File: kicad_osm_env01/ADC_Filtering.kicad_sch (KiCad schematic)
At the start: 16 parts

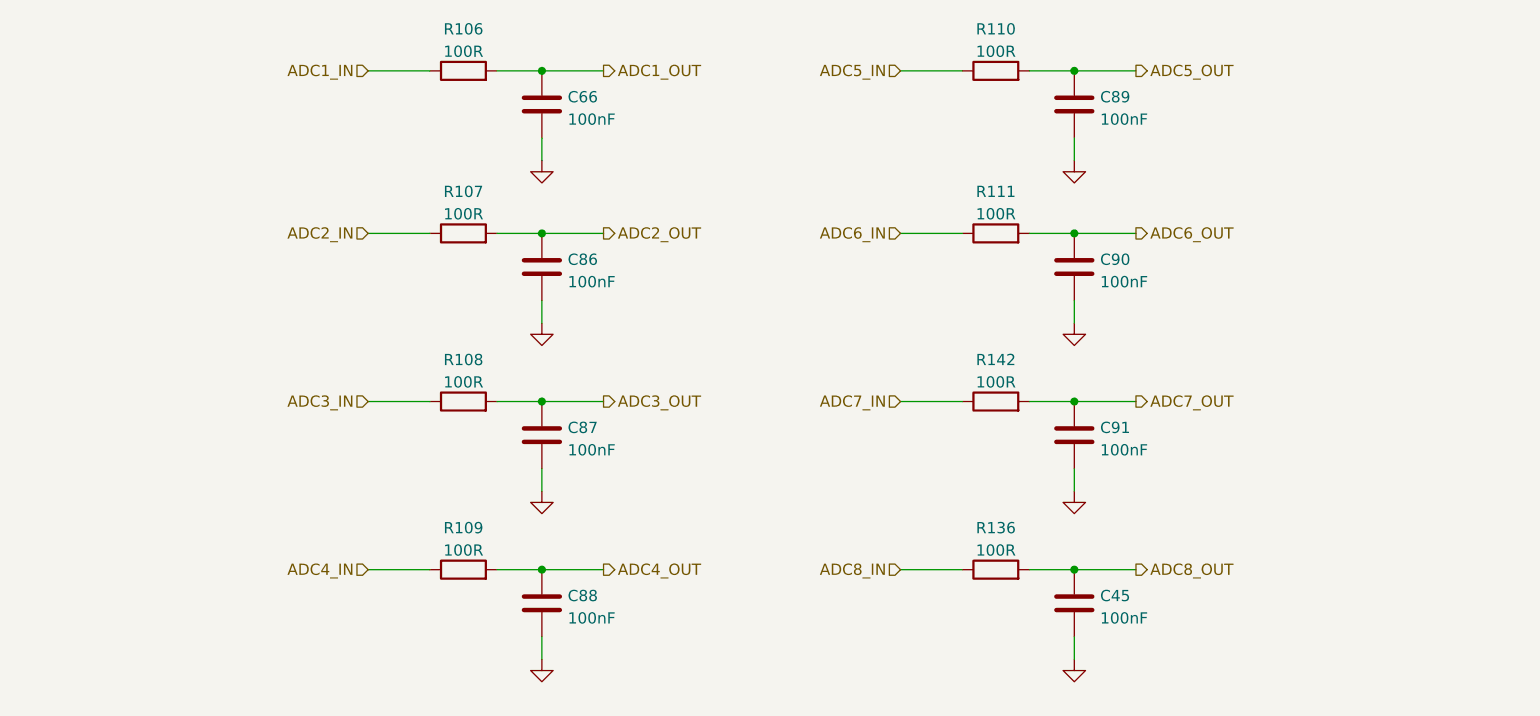
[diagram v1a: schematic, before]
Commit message: removed io module and 5V regulator
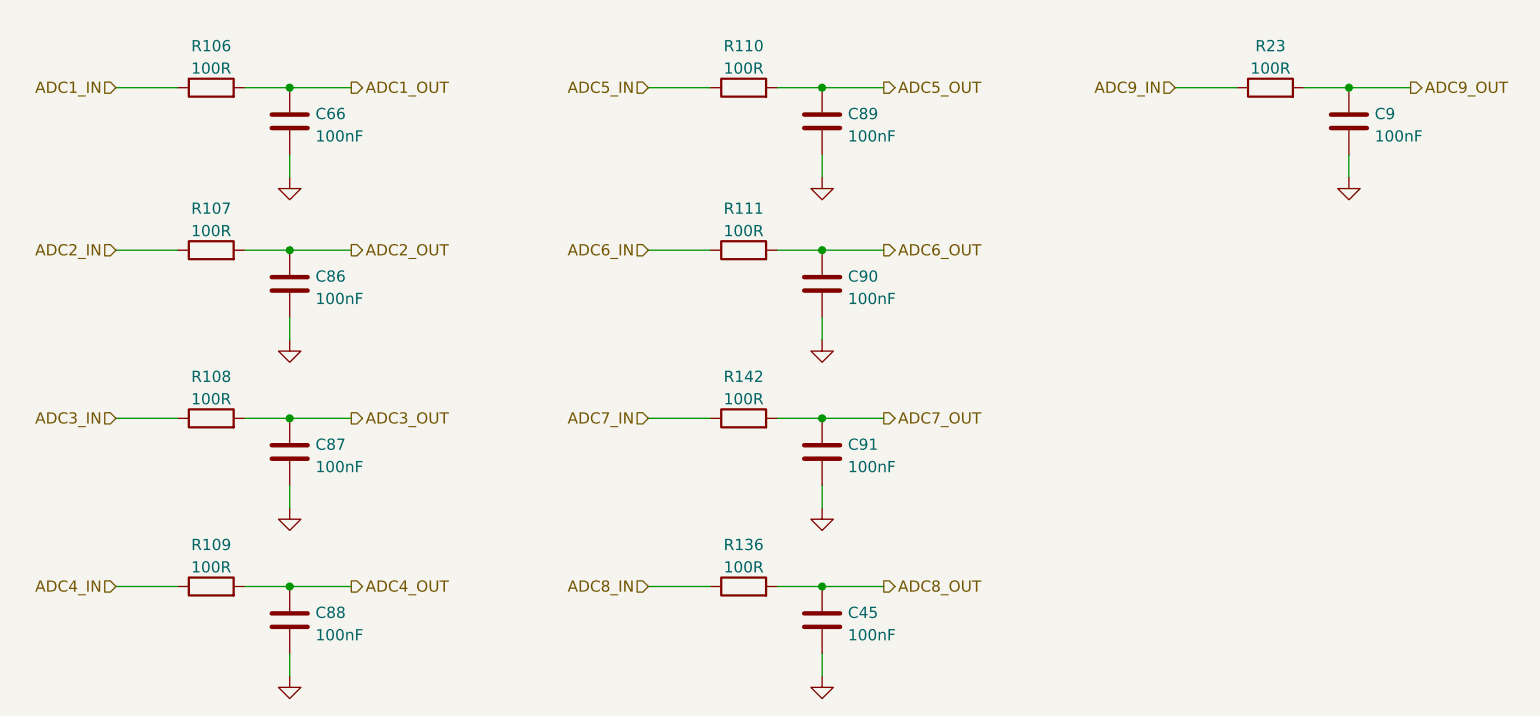
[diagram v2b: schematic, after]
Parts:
- added C9: 100nF, Capacitor_SMD:C_0402_1005Metric, symbol Device:C
- added R23: 100R, Resistor_SMD:R_0603_1608Metric, symbol Device:R
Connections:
- net GND: now also C9.2
- new net ADC9_IN: R23.1
- new net ADC9_OUT: C9.1, R23.2
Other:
- moved on the sheet: C45, C66, C86, C87, C88, C89, C90, C91, R106, R107, R108, R109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

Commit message: updated schematics with 5V ored circuit and new 3v3 regulator
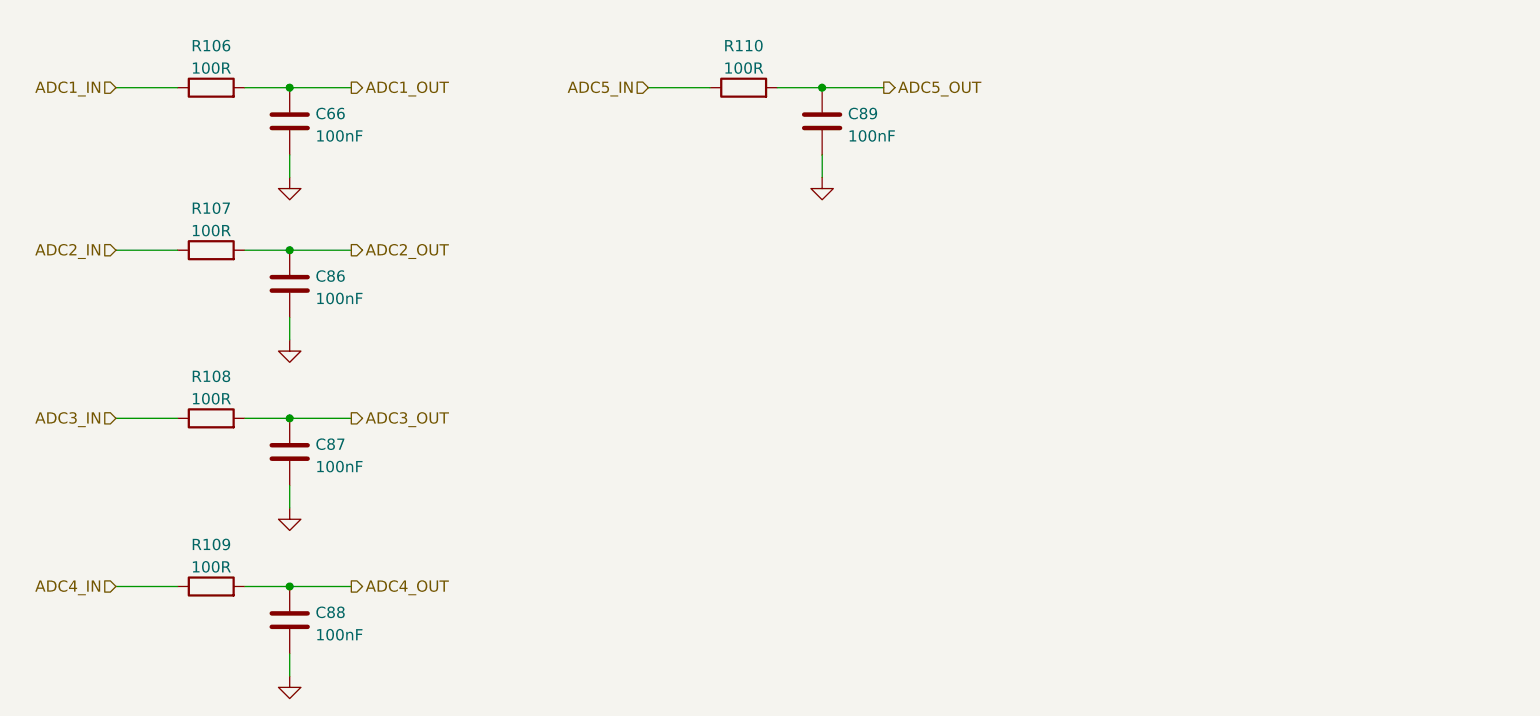
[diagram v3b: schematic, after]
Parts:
- removed C45, C9, C90, C91: 100nF, Capacitor_SMD:C_0402_1005Metric, symbol Device:C
- removed R111, R136, R142, R23: 100R, Resistor_SMD:R_0603_1608Metric, symbol Device:R

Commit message: assigned all footprints
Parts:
- C66, C86, C87, C88, C89: Voltage (none) -> 50V
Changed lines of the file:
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@@
   (title_block
     (title "Open Smart Monitor")
-    (date "2022-09-26")
-    (rev "C")
+    (date "2023-09-29")
+    (rev "C.2")
     (company "Devtank LTD")
     (comment 1 "Part No: 304-010")
@@
       (effects (font (size 1.27 1.27)) hide)
     )
-    (property "Datasheet" "~" (at 41.275 26.67 0)
+    (property "Datasheet" "" (at 41.275 26.67 0)
       (effects (font (size 1.27 1.27)) hide)
     )
@@
       (effects (font (size 1.27 1.27)) hide)
     )
-    (property "Datasheet" "~" (at 50.165 48.895 0)
+    (property "Datasheet" "" (at 50.165 48.895 0)
+      (effects (font (size 1.27 1.27)) hide)
+    )
+    (property "Voltage" "50V" (at 50.165 48.895 0)
       (effects (font (size 1.27 1.27)) hide)
     )
@@
       (effects (font (size 1.27 1.27)) hide)
     )
-    (property "Datasheet" "~" (at 101.6 26.67 0)
+    (property "Datasheet" "" (at 101.6 26.67 0)
       (effects (font (size 1.27 1.27)) hide)
     )
@@
       (effects (font (size 1.27 1.27)) hide)
     )
-    (property "Datasheet" "~" (at 41.275 64.135 0)
+    (property "Datasheet" "" (at 41.275 64.135 0)
       (effects (font (size 1.27 1.27)) hide)
     )
@@
       (effects (font (size 1.27 1.27)) hide)
     )
-    (property "Datasheet" "~" (at 41.275 83.185 0)
+    (property "Datasheet" "" (at 41.275 83.185 0)
       (effects (font (size 1.27 1.27)) hide)
     )
@@
       (effects (font (size 1.27 1.27)) hide)
     )
-    (property "Datasheet" "~" (at 50.165 30.48 0)
+    (property "Datasheet" "" (at 50.165 30.48 0)
+      (effects (font (size 1.27 1.27)) hide)
+    )
+    (property "Voltage" "50V" (at 50.165 30.48 0)
       (effects (font (size 1.27 1.27)) hide)
     )
@@
       (effects (font (size 1.27 1.27)) hide)
     )
-    (property "Datasheet" "~" (at 50.165 67.945 0)
+    (property "Datasheet" "" (at 50.165 67.945 0)
+      (effects (font (size 1.27 1.27)) hide)
+    )
+    (property "Voltage" "50V" (at 50.165 67.945 0)
       (effects (font (size 1.27 1.27)) hide)
     )
@@
       (effects (font (size 1.27 1.27)) hide)
     )
-    (property "Datasheet" "~" (at 50.165 86.995 0)
+    (property "Datasheet" "" (at 50.165 86.995 0)
+      (effects (font (size 1.27 1.27)) hide)
+    )
+    (property "Voltage" "50V" (at 50.165 86.995 0)
       (effects (font (size 1.27 1.27)) hide)
     )
@@
       (effects (font (size 1.27 1.27)) hide)
     )
-    (property "Datasheet" "~" (at 110.49 30.48 0)
+    (property "Datasheet" "" (at 110.49 30.48 0)
+      (effects (font (size 1.27 1.27)) hide)
+    )
+    (property "Voltage" "50V" (at 110.49 30.48 0)
       (effects (font (size 1.27 1.27)) hide)
     )
@@
       (effects (font (size 1.27 1.27)) hide)
     )
-    (property "Datasheet" "~" (at 41.275 45.085 0)
-      (effects (font (size 1.27 1.27)) hide)
-    )
+    (property "Datasheet" "" (at 41.275 45.085 0)
+      (effects (font (size 1.27 1.27)) hide)
+    )

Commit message: added information to symbol entries table, added jumper settings table, minor single track update on layout
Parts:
- C66, C86, C87, C88, C89: Characteristics (none) -> X5R; Other (none) -> Can use own part, but needs to meet the specs
- R106, R107, R108, R109, R110: Tolerance (none) -> 1%
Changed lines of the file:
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@@
+      (effects (font (size 1.27 1.27)) hide)
+    )
+    (property "Tolerance" "1%" (at 41.275 26.67 0)
+      (effects (font (size 1.27 1.27)) hide)
+    )
+    (property "Power Rating" "" (at 41.275 26.67 0)
+      (effects (font (size 1.27 1.27)) hide)
+    )
+    (property "Current Rating" "" (at 41.275 26.67 0)
       (effects (font (size 1.27 1.27)) hide)
     )
@@
       (effects (font (size 1.27 1.27)) hide)
     )
+    (property "Power Rating" "" (at 50.165 48.895 0)
+      (effects (font (size 1.27 1.27)) hide)
+    )
+    (property "Characteristics" "X5R" (at 50.165 48.895 0)
+      (effects (font (size 1.27 1.27)) hide)
+    )
+    (property "Current Rating" "" (at 50.165 48.895 0)
+      (effects (font (size 1.27 1.27)) hide)
+    )
+    (property "Other" "Can use own part, but needs to meet the specs" (at 50.165 48.895 0)
+      (effects (font (size 1.27 1.27)) hide)
+    )
     (pin "1")
     (pin "2")
@@
       (effects (font (size 1.27 1.27)) hide)
     )
+    (property "Tolerance" "1%" (at 101.6 26.67 0)
+      (effects (font (size 1.27 1.27)) hide)
+    )
+    (property "Power Rating" "" (at 101.6 26.67 0)
+      (effects (font (size 1.27 1.27)) hide)
+    )
+    (property "Current Rating" "" (at 101.6 26.67 0)
+      (effects (font (size 1.27 1.27)) hide)
+    )
     (pin "1")
     (pin "2")
@@
       (effects (font (size 1.27 1.27)) hide)
     )
+    (property "Tolerance" "1%" (at 41.275 64.135 0)
+      (effects (font (size 1.27 1.27)) hide)
+    )
+    (property "Power Rating" "" (at 41.275 64.135 0)
+      (effects (font (size 1.27 1.27)) hide)
+    )
+    (property "Current Rating" "" (at 41.275 64.135 0)
+      (effects (font (size 1.27 1.27)) hide)
+    )
     (pin "1")
     (pin "2")
@@
       (effects (font (size 1.27 1.27)) hide)
     )
+    (property "Tolerance" "1%" (at 41.275 83.185 0)
+      (effects (font (size 1.27 1.27)) hide)
+    )
+    (property "Power Rating" "" (at 41.275 83.185 0)
+      (effects (font (size 1.27 1.27)) hide)
+    )
+    (property "Current Rating" "" (at 41.275 83.185 0)
+      (effects (font (size 1.27 1.27)) hide)
+    )
     (pin "1")
     (pin "2")
@@
       (effects (font (size 1.27 1.27)) hide)
     )
+    (property "Power Rating" "" (at 50.165 30.48 0)
+      (effects (font (size 1.27 1.27)) hide)
+    )
+    (property "Characteristics" "X5R" (at 50.165 30.48 0)
+      (effects (font (size 1.27 1.27)) hide)
+    )
+    (property "Current Rating" "" (at 50.165 30.48 0)
+      (effects (font (size 1.27 1.27)) hide)
+    )
+    (property "Other" "Can use own part, but needs to meet the specs" (at 50.165 30.48 0)
+      (effects (font (size 1.27 1.27)) hide)
+    )
     (pin "1")
     (pin "2")
@@
       (effects (font (size 1.27 1.27)) hide)
     )
+    (property "Power Rating" "" (at 50.165 67.945 0)
+      (effects (font (size 1.27 1.27)) hide)
+    )
+    (property "Characteristics" "X5R" (at 50.165 67.945 0)
+      (effects (font (size 1.27 1.27)) hide)
+    )
+    (property "Current Rating" "" (at 50.165 67.945 0)
+      (effects (font (size 1.27 1.27)) hide)
+    )
+    (property "Other" "Can use own part, but needs to meet the specs" (at 50.165 67.945 0)
+      (effects (font (size 1.27 1.27)) hide)
+    )
     (pin "1")
     (pin "2")
@@
       (effects (font (size 1.27 1.27)) hide)
     )
+    (property "Power Rating" "" (at 50.165 86.995 0)
+      (effects (font (size 1.27 1.27)) hide)
+    )
+    (property "Characteristics" "X5R" (at 50.165 86.995 0)
+      (effects (font (size 1.27 1.27)) hide)
+    )
+    (property "Current Rating" "" (at 50.165 86.995 0)
+      (effects (font (size 1.27 1.27)) hide)
+    )
+    (property "Other" "Can use own part, but needs to meet the specs" (at 50.165 86.995 0)
+      (effects (font (size 1.27 1.27)) hide)
+    )
     (pin "1")
     (pin "2")
@@
       (effects (font (size 1.27 1.27)) hide)
     )
+    (property "Power Rating" "" (at 110.49 30.48 0)
+      (effects (font (size 1.27 1.27)) hide)
+    )
+    (property "Characteristics" "X5R" (at 110.49 30.48 0)
+      (effects (font (size 1.27 1.27)) hide)
+    )
+    (property "Current Rating" "" (at 110.49 30.48 0)
+      (effects (font (size 1.27 1.27)) hide)
+    )
+    (property "Other" "Can use own part, but needs to meet the specs" (at 110.49 30.48 0)
+      (effects (font (size 1.27 1.27)) hide)
+    )
     (pin "1")
     (pin "2")
@@
       (effects (font (size 1.27 1.27)) hide)
     )
+    (property "Tolerance" "1%" (at 41.275 45.085 0)
+      (effects (font (size 1.27 1.27)) hide)
+    )
+    (property "Power Rating" "" (at 41.275 45.085 0)
+      (effects (font (size 1.27 1.27)) hide)
+    )
+    (property "Current Rating" "" (at 41.275 45.085 0)
+      (effects (font (size 1.27 1.27)) hide)
+    )

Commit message: minor update to layout
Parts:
- R106, R107, R108, R109, R110: Other (none) -> Can use own part, but needs to meet the specs
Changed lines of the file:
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@@
+      (effects (font (size 1.27 1.27)) hide)
+    )
+    (property "Other" "Can use own part, but needs to meet the specs" (at 41.275 26.67 0)
       (effects (font (size 1.27 1.27)) hide)
     )
@@
       (effects (font (size 1.27 1.27)) hide)
     )
+    (property "Other" "Can use own part, but needs to meet the specs" (at 101.6 26.67 0)
+      (effects (font (size 1.27 1.27)) hide)
+    )
     (pin "1")
     (pin "2")
@@
       (effects (font (size 1.27 1.27)) hide)
     )
+    (property "Other" "Can use own part, but needs to meet the specs" (at 41.275 64.135 0)
+      (effects (font (size 1.27 1.27)) hide)
+    )
     (pin "1")
     (pin "2")
@@
       (effects (font (size 1.27 1.27)) hide)
     )
+    (property "Other" "Can use own part, but needs to meet the specs" (at 41.275 83.185 0)
+      (effects (font (size 1.27 1.27)) hide)
+    )
     (pin "1")
     (pin "2")
@@
       (effects (font (size 1.27 1.27)) hide)
     )
+    (property "Other" "Can use own part, but needs to meet the specs" (at 41.275 45.085 0)
+      (effects (font (size 1.27 1.27)) hide)
+    )
